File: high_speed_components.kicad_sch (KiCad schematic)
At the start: 19 parts, among them J1 USB_C_Receptacle, U1 HD3SS3220RNHR

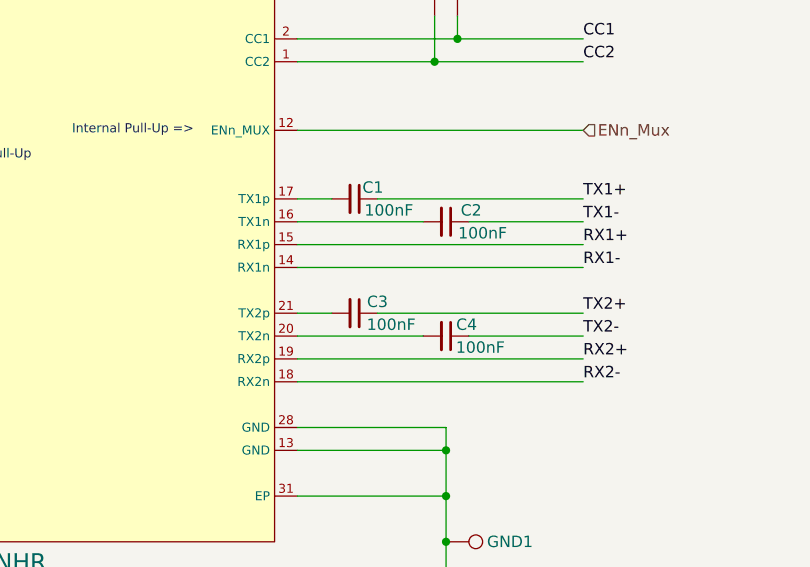
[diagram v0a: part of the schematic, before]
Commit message: Routing Complete (DRC Checker Errors needs fixing)
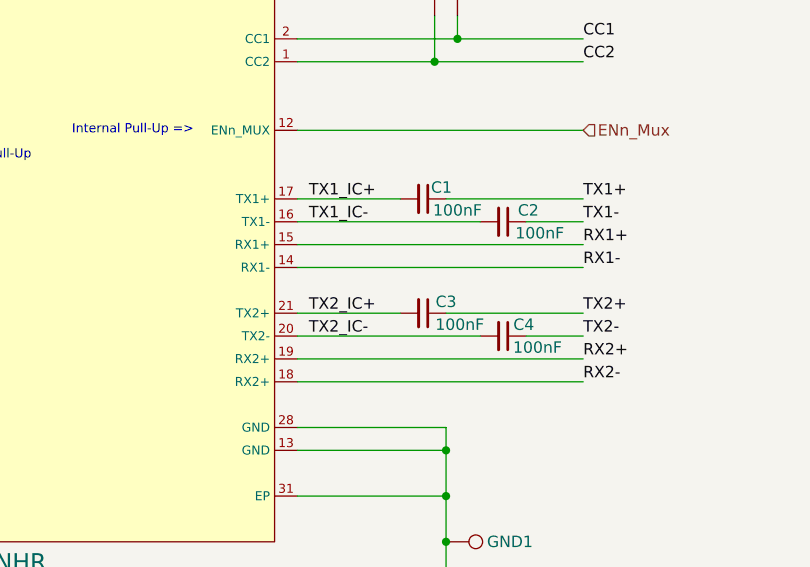
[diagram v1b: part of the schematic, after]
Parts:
- C1, C2, C3, C4, C5, C6: footprint Capacitor_SMD:C_0603_1608Metric -> Capacitor_SMD:C_0402_1005Metric
- J1: footprint to-be-organized:USB-C-SMD_TYPE-C-USB-19 -> Interface_USB:USB-C-SMD_TYPE-C-USB-19
- R1, R2: footprint Resistor_SMD:R_0603_1608Metric -> Resistor_SMD:R_0402_1005Metric
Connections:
- net TX2_IC-: now reaches C4.2, U1.20 (TX2-)
- net TX2_IC+: now reaches C3.2, U1.21 (TX2+)
- net TX1_IC-: now reaches C2.2, U1.16 (TX1-)
- net TX1_IC+: now reaches C1.2, U1.17 (TX1+)
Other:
- moved on the sheet: C1, C2, C3, C4
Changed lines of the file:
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@@
 	(wire
 		(pts
-			(xy 139.7 106.68) (xy 153.67 106.68)
-		)
-		(stroke
-			(width 0)
-			(type default)
-		)
-	)
-	(wire
-		(pts
-			(xy 158.75 106.68) (xy 171.45 106.68)
+			(xy 139.7 106.68) (xy 160.02 106.68)
+		)
+		(stroke
+			(width 0)
+			(type default)
+		)
+	)
+	(wire
+		(pts
+			(xy 165.1 106.68) (xy 171.45 106.68)
 		)
 		(stroke
@@
 	(wire
 		(pts
-			(xy 158.75 93.98) (xy 171.45 93.98)
+			(xy 165.1 93.98) (xy 171.45 93.98)
 		)
 		(stroke
@@
 	(wire
 		(pts
-			(xy 139.7 91.44) (xy 143.51 91.44)
+			(xy 139.7 91.44) (xy 151.13 91.44)
 		)
 		(stroke
@@
 	(wire
 		(pts
-			(xy 148.59 104.14) (xy 171.45 104.14)
+			(xy 156.21 104.14) (xy 171.45 104.14)
 		)
 		(stroke
@@
 	(wire
 		(pts
-			(xy 139.7 104.14) (xy 143.51 104.14)
+			(xy 139.7 104.14) (xy 151.13 104.14)
 		)
 		(stroke
@@
 	(wire
 		(pts
-			(xy 148.59 91.44) (xy 171.45 91.44)
-		)
-		(stroke
-			(width 0)
-			(type default)
-		)
-	)
-	(wire
-		(pts
-			(xy 139.7 93.98) (xy 153.67 93.98)
+			(xy 156.21 91.44) (xy 171.45 91.44)
+		)
+		(stroke
+			(width 0)
+			(type default)
+		)
+	)
+	(wire
+		(pts
+			(xy 139.7 93.98) (xy 160.02 93.98)
 		)
 		(stroke
@@
 			(width 0)
 			(type default)
+		)
+	)
+	(label "TX2_IC+"
+		(at 140.97 104.14 0)
+		(effects
+			(font
+				(size 1.27 1.27)
+			)
+			(justify left bottom)
 		)
 	)
@@
 		)
 	)
+	(label "TX1_IC+"
+		(at 140.97 91.44 0)
+		(effects
+			(font
+				(size 1.27 1.27)
+			)
+			(justify left bottom)
+		)
+	)
 	(label "RX2+"
 		(at 171.45 109.22 0)
@@
 		)
 	)
+	(label "TX2_IC-"
+		(at 140.97 106.68 0)
+		(effects
+			(font
+				(size 1.27 1.27)
+			)
+			(justify left bottom)
+		)
+	)
 	(label "TX1-"
 		(at 217.17 105.41 180)
@@
 	(label "TX1+"
 		(at 171.45 91.44 0)
+		(effects
+			(font
+				(size 1.27 1.27)
+			)
+			(justify left bottom)
+		)
+	)
+	(label "TX1_IC-"
+		(at 140.97 93.98 0)
 		(effects
 			(font
@@
 			)
 		)
-		(property "Footprint" "Resistor_SMD:R_0603_1608Metric"
+		(property "Footprint" "Resistor_SMD:R_0402_1005Metric"
 			(at 78.74 88.9 0)
 			(hide yes)
@@
 	(symbol
 		(lib_id "Device:C_Small")
-		(at 156.21 106.68 270)
+		(at 162.56 106.68 270)
 		(unit 1)
 		(body_style 1)
@@
 		(dnp no)
 		(property "Reference" "C4"
-			(at 158.496 105.41 90)
+			(at 164.846 105.41 90)
 			(show_name no)
 			(do_not_autoplace no)
@@
 		)
 		(property "Value" "100nF"
-			(at 160.02 107.95 90)
-			(show_name no)
-			(do_not_autoplace no)
-			(effects
-				(font
-					(size 1.27 1.27)
-				)
-			)
-		)
-		(property "Footprint" "Capacitor_SMD:C_0603_1608Metric"
-			(at 156.21 106.68 0)
+			(at 166.37 107.95 90)
+			(show_name no)
+			(do_not_autoplace no)
+			(effects
+				(font
+					(size 1.27 1.27)
+				)
+			)
+		)
+		(property "Footprint" "Capacitor_SMD:C_0402_1005Metric"
+			(at 162.56 106.68 0)
 			(hide yes)
 			(show_name no)
@@
 		)
 		(property "Datasheet" ""
-			(at 156.21 106.68 0)
+			(at 162.56 106.68 0)
 			(hide yes)
 			(show_name no)
@@
 		)
 		(property "Description" "Unpolarized capacitor, small symbol"
-			(at 156.21 106.68 0)
+			(at 162.56 106.68 0)
 			(hide yes)
 			(show_name no)
@@
 			)
 		)
-		(property "Footprint" "to-be-organized:USB-C-SMD_TYPE-C-USB-19"
+		(property "Footprint" "Interface_USB:USB-C-SMD_TYPE-C-USB-19"
 			(at 234.95 97.79 0)
 			(hide yes)
@@
 	(symbol
 		(lib_id "Device:C_Small")
-		(at 146.05 104.14 270)
+		(at 153.67 104.14 270)
 		(unit 1)
 		(body_style 1)
@@
 		(dnp no)
 		(property "Reference" "C3"
-			(at 148.59 102.87 90)
+			(at 156.21 102.87 90)
 			(show_name no)
 			(do_not_autoplace no)
@@
 		)
 		(property "Value" "100nF"
-			(at 150.114 105.41 90)
-			(show_name no)
-			(do_not_autoplace no)
-			(effects
-				(font
-					(size 1.27 1.27)
-				)
-			)
-		)
-		(property "Footprint" "Capacitor_SMD:C_0603_1608Metric"
-			(at 146.05 104.14 0)
+			(at 157.734 105.41 90)
+			(show_name no)
+			(do_not_autoplace no)
+			(effects
+				(font
+					(size 1.27 1.27)
+				)
+			)
+		)
+		(property "Footprint" "Capacitor_SMD:C_0402_1005Metric"
+			(at 153.67 104.14 0)
 			(hide yes)
 			(show_name no)
@@
 		)
 		(property "Datasheet" ""
-			(at 146.05 104.14 0)
+			(at 153.67 104.14 0)
 			(hide yes)
 			(show_name no)
@@
 		)
 		(property "Description" "Unpolarized capacitor, small symbol"
-			(at 146.05 104.14 0)
+			(at 153.67 104.14 0)
 			(hide yes)
 			(show_name no)
@@
 	(symbol
 		(lib_id "Device:C_Small")
-		(at 156.21 93.98 270)
+		(at 162.56 93.98 270)
 		(unit 1)
 		(body_style 1)
@@
 		(dnp no)
 		(property "Reference" "C2"
-			(at 159.004 92.71 90)
+			(at 165.354 92.71 90)
 			(show_name no)
 			(do_not_autoplace no)
@@
 		)
 		(property "Value" "100nF"
-			(at 160.274 95.25 90)
-			(show_name no)
-			(do_not_autoplace no)
-			(effects
-				(font
-					(size 1.27 1.27)
-				)
-			)
-		)
-		(property "Footprint" "Capacitor_SMD:C_0603_1608Metric"
-			(at 156.21 93.98 0)
+			(at 166.624 95.25 90)
+			(show_name no)
+			(do_not_autoplace no)
+			(effects
+				(font
+					(size 1.27 1.27)
+				)
+			)
+		)
+		(property "Footprint" "Capacitor_SMD:C_0402_1005Metric"
+			(at 162.56 93.98 0)
 			(hide yes)
 			(show_name no)
@@
 		)
 		(property "Datasheet" ""
-			(at 156.21 93.98 0)
+			(at 162.56 93.98 0)
 			(hide yes)
 			(show_name no)
@@
 		)
 		(property "Description" "Unpolarized capacitor, small symbol"
-			(at 156.21 93.98 0)
+			(at 162.56 93.98 0)
 			(hide yes)
 			(show_name no)
@@
 	(symbol
 		(lib_id "Device:C_Small")
-		(at 146.05 91.44 270)
+		(at 153.67 91.44 270)
 		(unit 1)
 		(body_style 1)
@@
 		(dnp no)
 		(property "Reference" "C1"
-			(at 148.082 90.17 90)
+			(at 155.702 90.17 90)
 			(show_name no)
 			(do_not_autoplace no)
@@
 		)
 		(property "Value" "100nF"
-			(at 149.86 92.71 90)
-			(show_name no)
-			(do_not_autoplace no)
-			(effects
-				(font
-					(size 1.27 1.27)
-				)
-			)
-		)
-		(property "Footprint" "Capacitor_SMD:C_0603_1608Metric"
-			(at 146.05 91.44 0)
+			(at 157.48 92.71 90)
+			(show_name no)
+			(do_not_autoplace no)
+			(effects
+				(font
+					(size 1.27 1.27)
+				)
+			)
+		)
+		(property "Footprint" "Capacitor_SMD:C_0402_1005Metric"
+			(at 153.67 91.44 0)
 			(hide yes)
 			(show_name no)
@@
 		)
 		(property "Datasheet" ""
-			(at 146.05 91.44 0)
+			(at 153.67 91.44 0)
 			(hide yes)
 			(show_name no)
@@
 		)
 		(property "Description" "Unpolarized capacitor, small symbol"
-			(at 146.05 91.44 0)
+			(at 153.67 91.44 0)
 			(hide yes)
 			(show_name no)
@@
 			)
 		)
-		(property "Footprint" "Resistor_SMD:R_0603_1608Metric"
+		(property "Footprint" "Resistor_SMD:R_0402_1005Metric"
 			(at 69.85 78.74 0)
 			(hide yes)
@@
 			)
 		)
-		(property "Footprint" "Capacitor_SMD:C_0603_1608Metric"
+		(property "Footprint" "Capacitor_SMD:C_0402_1005Metric"
 			(at 62.23 116.84 0)
 			(hide yes)
@@
 			)
 		)
-		(property "Footprint" "Capacitor_SMD:C_0603_1608Metric"
+		(property "Footprint" "Capacitor_SMD:C_0402_1005Metric"
 			(at 64.77 119.38 0)
 			(hide yes)

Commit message: DRC Errors Fixed, BOM Cleaned up and Generated, Gerber Generated
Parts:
- C1, C2, C3, C4, C5, C6: LCSC (none) -> C106204; Store Page (none) -> https://www.lcsc.com/product-detail/C106204.html; Unit Price (none) -> 0.0016
- DIR_LED1, VBUS_LED1: LCSC (none) -> C375576; Store Page (none) -> https://www.lcsc.com/product-detail/C375576.html; Unit Price (none) -> 0.0305
- J1: LCSC (none) -> C2765186; Store Page (none) -> https://www.lcsc.com/product-detail/C22359725.html; Unit Price (none) -> 1.1587
- R1: footprint Resistor_SMD:R_0402_1005Metric -> Resistor_SMD:R_0805_2012Metric; LCSC (none) -> C52209984; Store Page (none) -> https://www.lcsc.com/product-detail/C52209984.html; Unit Price (none) -> 0.0026
- R2: LCSC (none) -> C413111; Store Page (none) -> https://item.szlcsc.com/405106.html; Unit Price (none) -> 0.0078
- U1: Store Page (none) -> https://item.szlcsc.com/176537.html; Unit Price (none) -> 1.9468
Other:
- company: (none) -> UWaterloo Reality Labs
- title: (none) -> USB-3.0 Bridging Board High-Speed Interface
